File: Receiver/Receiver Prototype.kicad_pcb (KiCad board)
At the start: 4 copper layers, 35 parts, among them J1 Conn_01x02_Socket, J2 Conn_01x03, J4 Conn_Coaxial, J5 Conn_01x02, J6 Conn_01x02, J7 Conn_Coaxial, J8 Conn_Coaxial, U1 OPA3692ID, U2 AD8692ARZ

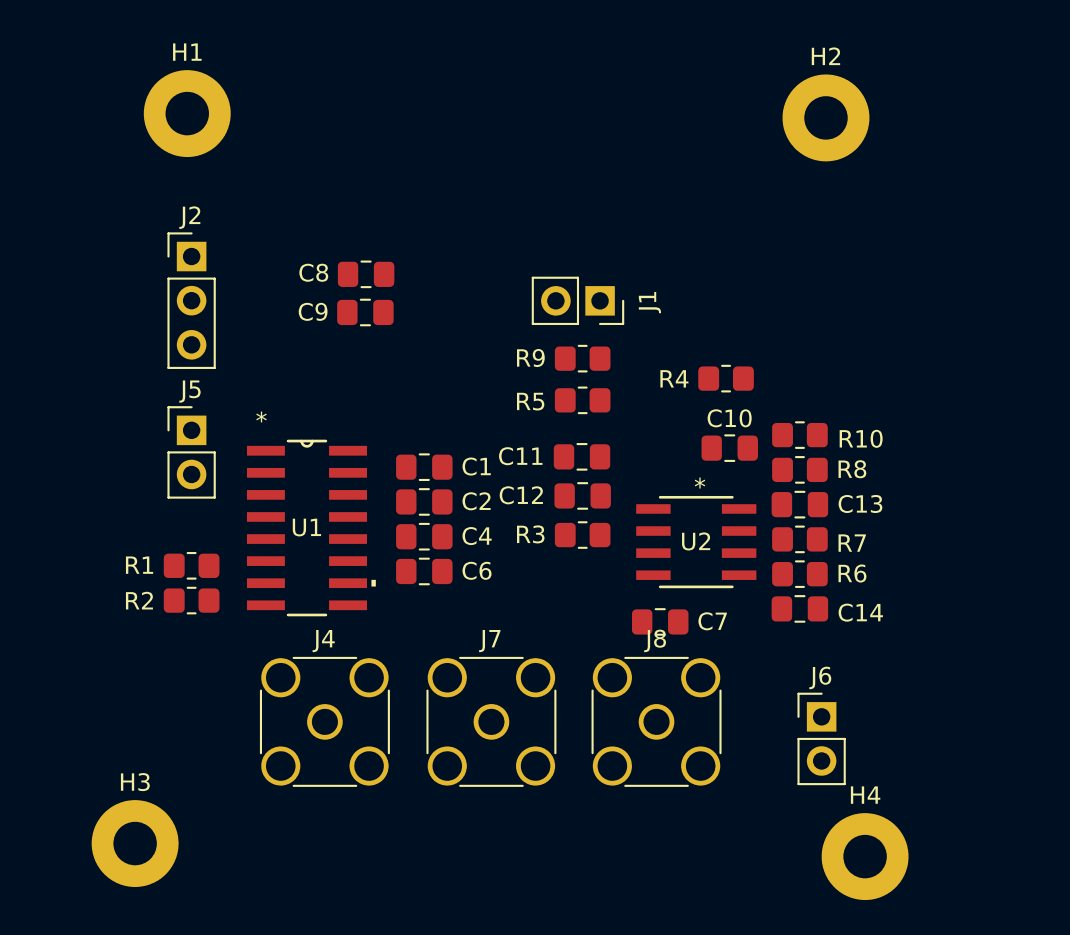
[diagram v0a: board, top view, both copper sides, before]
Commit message: Receiver PCB design v1 complete. DRC passed. Component's lables not added
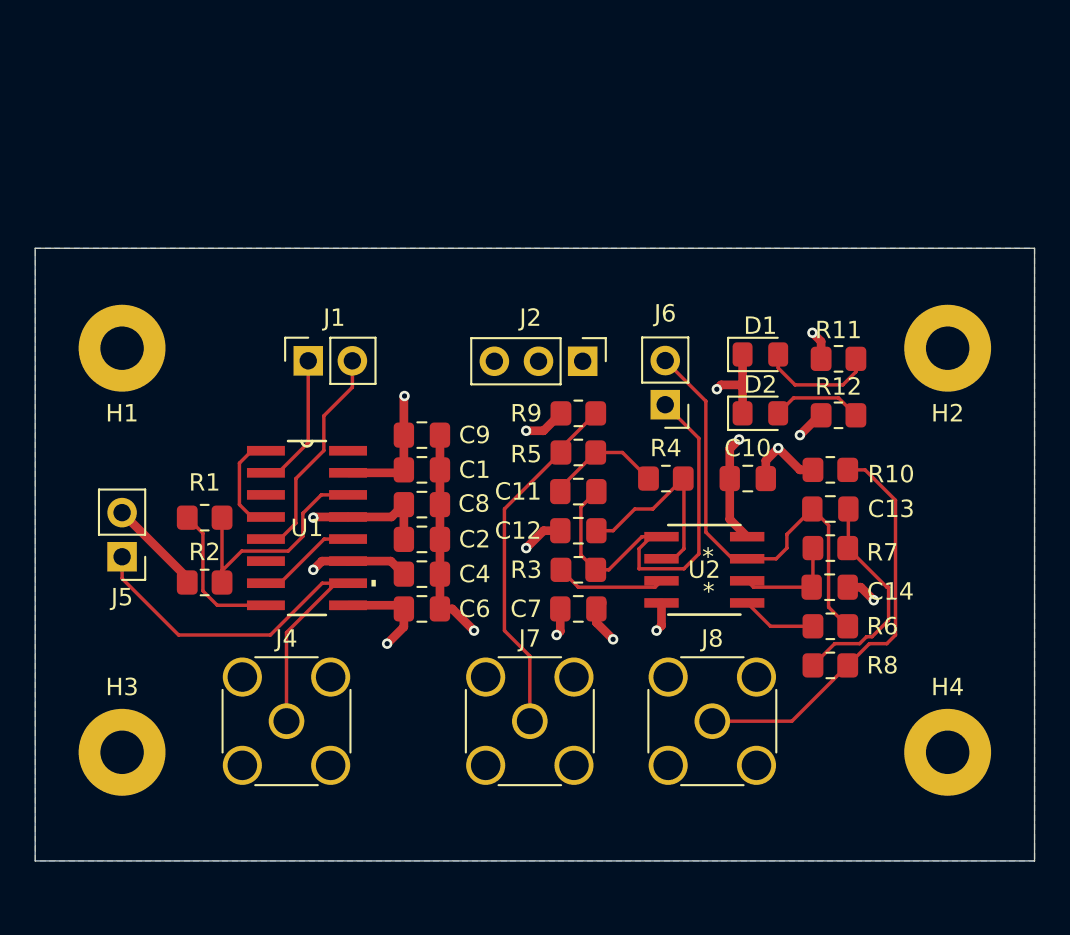
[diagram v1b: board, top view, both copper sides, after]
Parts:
- added D1: LED, LED_SMD:LED_0805_2012Metric_Pad1.15x1.40mm_HandSolder, F.Cu at (191.7, 73.4)
- added D2: LED, LED_SMD:LED_0805_2012Metric_Pad1.15x1.40mm_HandSolder, F.Cu at (191.7, 76.7)
- added R11: R, Resistor_SMD:R_0805_2012Metric_Pad1.20x1.40mm_HandSolder, F.Cu at (196.2, 73.6)
- added R12: R, Resistor_SMD:R_0805_2012Metric_Pad1.20x1.40mm_HandSolder, F.Cu at (196.2, 76.9)
- moved J2 23.3 mm to (181.5, 73.8), turned to -90 degrees
- moved J6 20.1 mm to (186.2, 76.2), turned to 180 degrees
- moved J1 17.1 mm to (165.7, 73.7), turned to 90 degrees
- moved H2 15.0 mm to (202.5, 73.0)
- moved H1 14.0 mm to (155.0, 73.0)
- moved C8 13.6 mm to (172.2, 82.0)
- moved R8 11.4 mm to (195.8, 91.2)
- moved J5 8.30 mm to (155.0, 85.0), turned to 180 degrees
- moved C9 7.77 mm to (172.2, 78.0)
- moved H4 7.65 mm to (202.5, 96.2)
- moved R4 6.71 mm to (186.3, 80.5)
- moved H3 5.30 mm to (155.0, 96.2)
- moved C7 4.77 mm to (181.2, 88.0), turned to 180 degrees
- moved R6 3.47 mm to (195.8, 89.0)
- moved J8 3.21 mm to (189.0, 94.5)
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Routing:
- net GND: track 0.00 -> 35.8 mm, vias 0 -> 7
- net /Q_Filter_Out: track 0.00 -> 26.8 mm
- net /Inst_Out: track 0.00 -> 26.6 mm
- net /I_Filter_Out: track 0.00 -> 25.7 mm
- net /Q_Filter_In: track 0.00 -> 23.8 mm
- net VCC: track 0.00 -> 21.2 mm, vias 0 -> 4
- net /I_Filter_In: track 0.00 -> 20.5 mm
- net VEE: track 0.00 -> 19.3 mm, vias 0 -> 5
- net Net-(U1-OUTA): track 0.00 -> 14.2 mm
- net Net-(C13-Pad2): track 0.00 -> 12.9 mm
- net /INB: track 0.00 -> 12.8 mm
- net Net-(U2--INA): track 0.00 -> 11.8 mm
- net Net-(U1-INC+): track 0.00 -> 8.55 mm
- net /INA: track 0.00 -> 7.86 mm
- net Net-(C11-Pad2): track 0.00 -> 6.75 mm
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- added copper zone on In1.Cu, net GND
- added copper zone on In2.Cu, net VCC
- added copper zone on B.Cu, net VEE
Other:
- board outline added: 57.5 x 35.2 mm

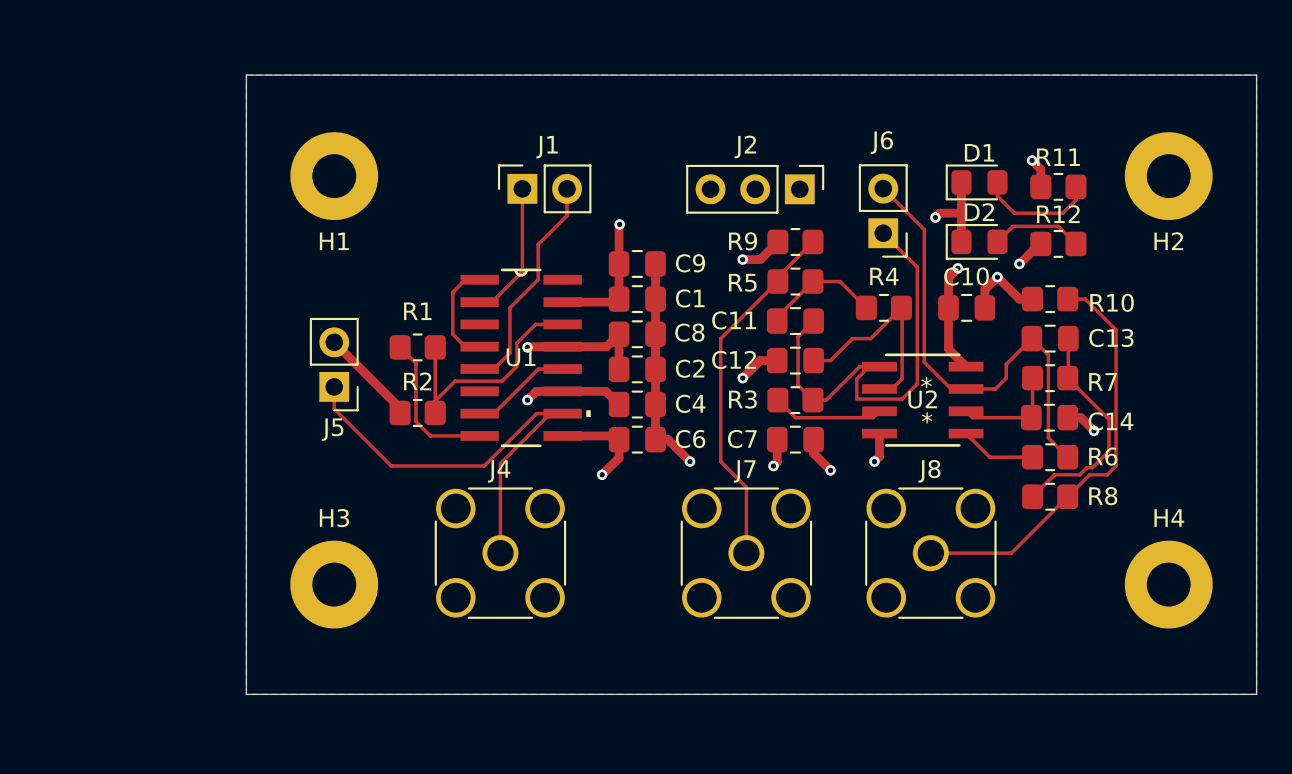
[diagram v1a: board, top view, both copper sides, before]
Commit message: This revision includes BNC connectors, SSOP packages, minor fixes and some basic lables
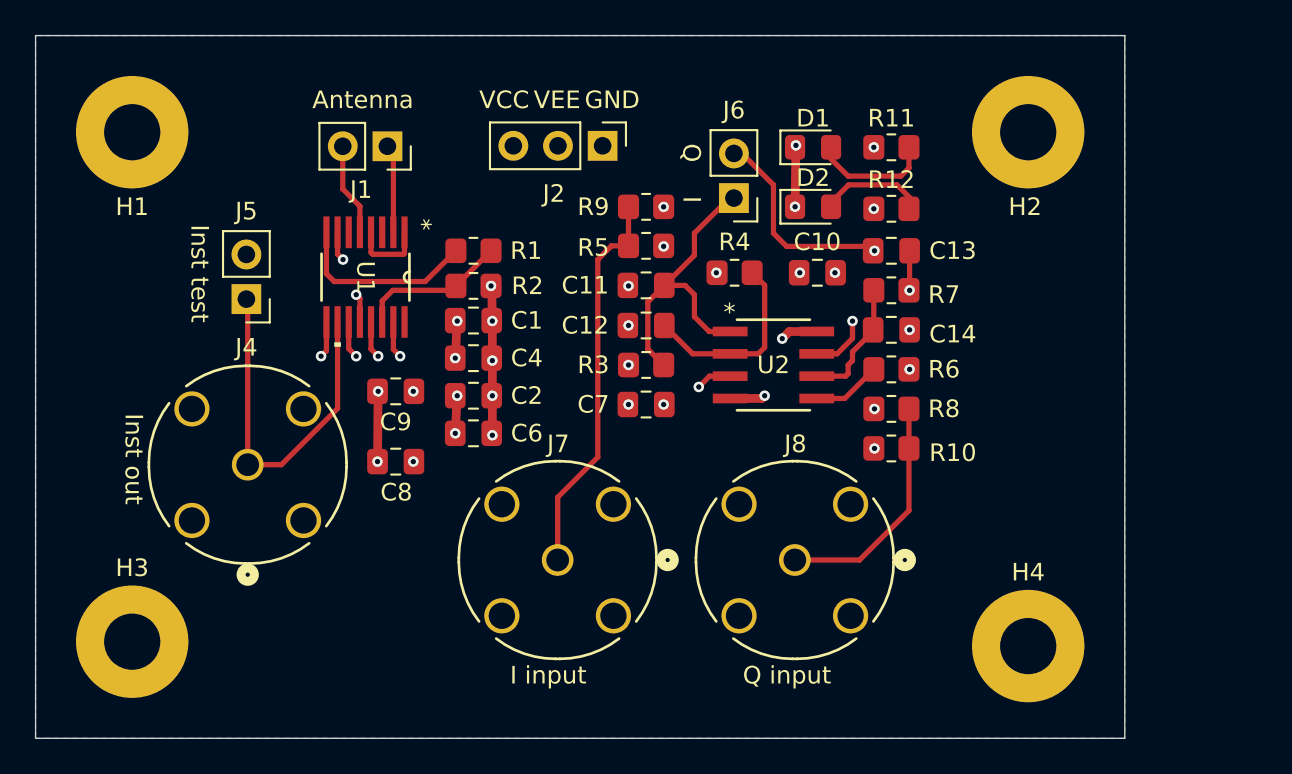
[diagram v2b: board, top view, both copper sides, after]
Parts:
- H1, H2, H3, H4: footprint MountingHole:MountingHole_2.5mm_Pad -> MountingHole:MountingHole_3.2mm_M3_Pad
- J4, J7, J8: footprint Connector_Coaxial:SMA_Amphenol_132134_Vertical -> BNC 112404:CONN_112404_AMP
- R11, R12: value R -> 4.7k
- U1: footprint OPA3692ID:D16 -> OPA3692 SSOP:DBQ16
- moved C8 15.5 mm to (158.5, 89.2), turned to 180 degrees
- moved C9 15.5 mm to (158.5, 85.2), turned to 180 degrees
- moved J4 15.2 mm to (150.1, 89.4), turned to -90 degrees
- moved R10 12.4 mm to (186.7, 88.5)
- moved H3 12.0 mm to (143.5, 99.5)
- moved H1 11.8 mm to (143.5, 70.5)
- moved J2 11.5 mm to (170.3, 71.3)
- moved J7 10.8 mm to (167.7, 94.8)
- moved C13 10.3 mm to (186.7, 77.2)
- moved R6 10.3 mm to (186.7, 84.0)
- moved R7 10.3 mm to (186.7, 79.5)
- moved R8 10.3 mm to (186.7, 86.2)
- moved C14 10.3 mm to (186.7, 81.8)
- moved U1 9.98 mm to (156.8, 78.8), turned to -90 degrees
- moved R11 9.77 mm to (186.7, 71.4)
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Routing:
- net GND: track 35.8 -> 16.3 mm, vias 7 -> 15
- net VCC: track 21.2 -> 8.82 mm, vias 4 -> 8
- net VEE: track 19.3 -> 8.55 mm, vias 5 -> 8
- net /Q_Filter_In: track 23.8 -> 13.4 mm
- net /I_Filter_Out: track 25.7 -> 17.6 mm
- net /INB: track 12.8 -> 5.30 mm
- net /Inst_Out: track 26.6 -> 20.8 mm
- net Net-(U1-OUTA): track 14.2 -> 8.58 mm
- net /INA: track 7.86 -> 5.04 mm
- net Net-(U1-INC+): track 8.55 -> 10.6 mm
- net /I_Filter_In: track 20.5 -> 22.3 mm
- net Net-(U1-INA-): track 6.03 -> 4.32 mm
- net Net-(C13-Pad2): track 12.9 -> 11.8 mm, vias 0 -> 2
- net Net-(U2--INB): track 6.14 -> 7.20 mm
- net /Q_Filter_Out: track 26.8 -> 25.8 mm, vias 0 -> 3
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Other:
- board size 57.5 x 35.2 mm -> 62 x 40 mm
- board text added: "Antenna"
- board text added: "GND"
- board text added: "I"
- board text added: "I input"
- board text added: "Inst out"
- board text added: "Inst test"
- board text added: "Q"
- board text added: "Q input"
- board text added: "VCC"
- board text added: "VEE"

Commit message: minor fixes
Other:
- board text added: "Coil"
- board text removed: "Antenna"
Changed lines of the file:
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@@
 		)
 	)
-	(gr_text "Antenna\n"
-		(at 153.75 69.25 0)
+	(gr_text "Coil"
+		(at 155.275119 69.25 0)
 		(layer "F.SilkS")
 		(effects

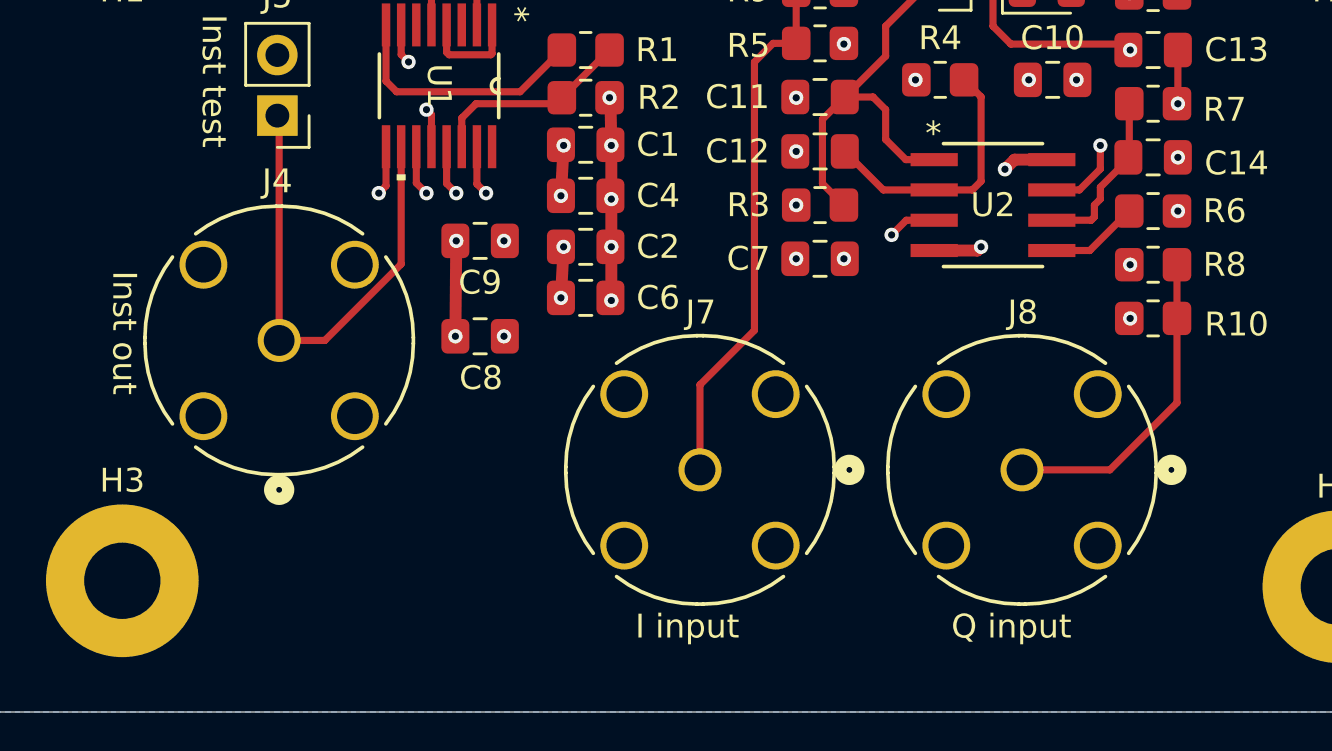
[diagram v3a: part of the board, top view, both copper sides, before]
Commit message: Added 3D models
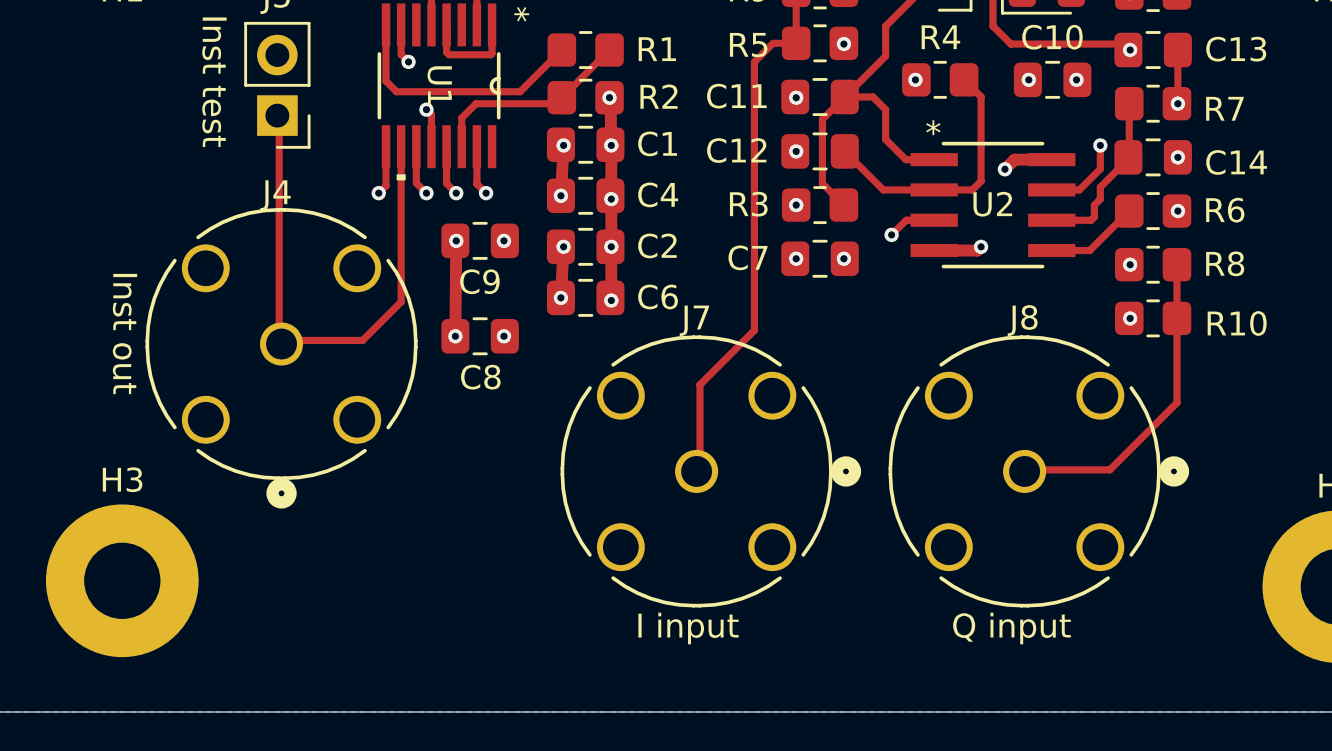
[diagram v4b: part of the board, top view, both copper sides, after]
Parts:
- R1: value 200 -> 200
- moved J4 0.18 mm to (150.2, 89.6)
- moved J7 0.16 mm to (167.6, 94.9)
- moved J8 0.13 mm to (181.3, 94.9)
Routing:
- net /Inst_Out: track 20.8 -> 21.7 mm
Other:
- board text added: "Receiver 1.0 2024-04-01"
